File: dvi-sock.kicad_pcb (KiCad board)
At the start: 2 copper layers, 25.2 x 22.5 mm, 12 parts, among them J1 Conn_01x05, J2 Conn_01x05, J3 Conn_01x03, J4 NOT_HDMI_A

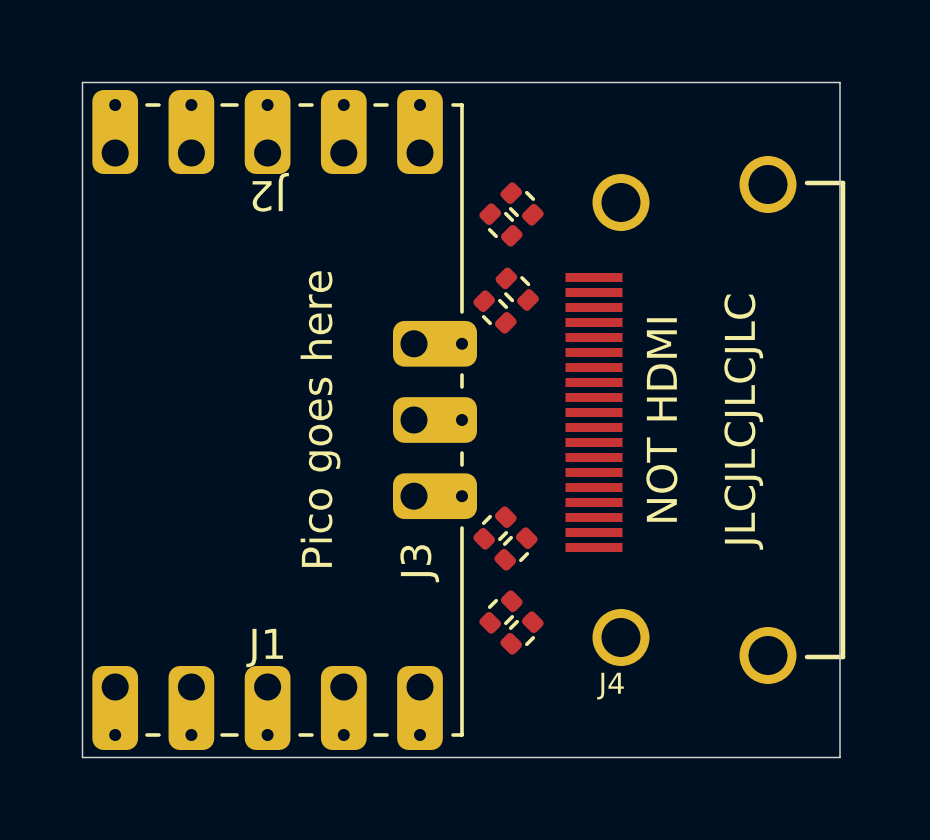
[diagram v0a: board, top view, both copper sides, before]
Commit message: Routed, DRC clean
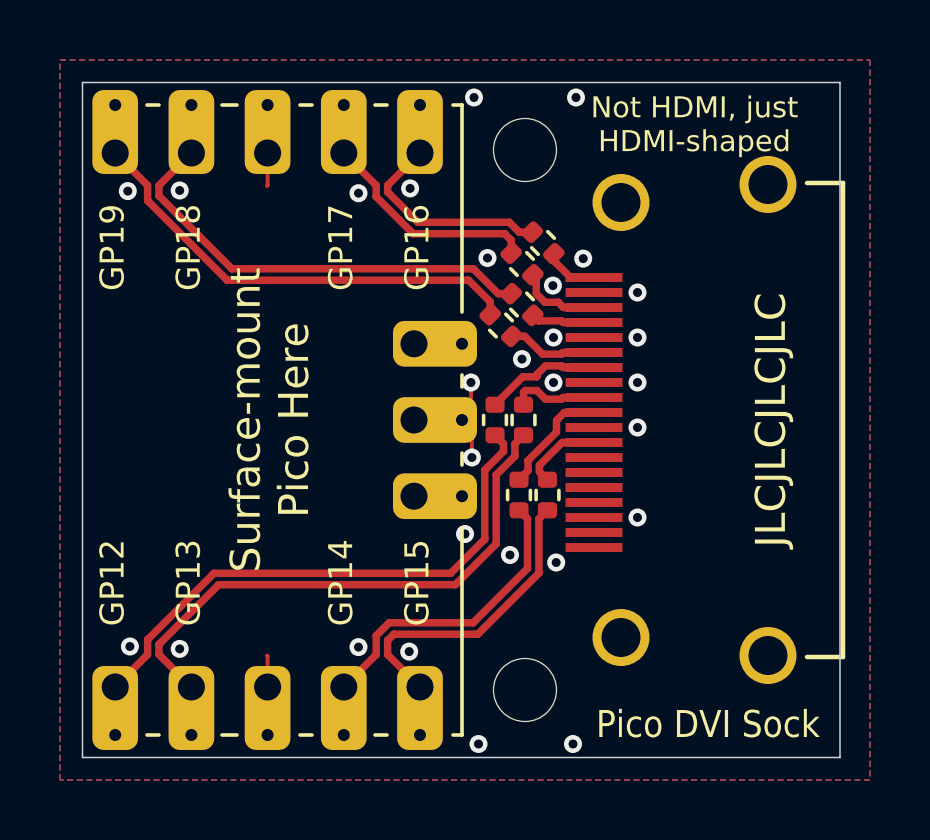
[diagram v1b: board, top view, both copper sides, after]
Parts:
- added REF**: MH_Pico_M2ish, dvi-sock:MH_Pico_M2ish, F.Cu at (156.5, 94.0)
- added REF**: MH_Pico_M2ish, dvi-sock:MH_Pico_M2ish, F.Cu at (156.5, 76.0)
- moved R8 4.68 mm to (157.2, 87.5), turned to 90 degrees
- moved R6 4.31 mm to (156.4, 85.0), turned to 90 degrees
- moved R7 3.95 mm to (156.3, 87.5), turned to 90 degrees
- moved R5 3.60 mm to (155.5, 85.0), turned to 90 degrees
- moved R2 1.48 mm to (156.4, 79.8)
- moved R1 1.48 mm to (157.1, 79.1)
- moved R3 0.54 mm to (156.4, 81.2)
- moved R4 0.49 mm to (155.7, 81.8)
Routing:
- net /PICO_D0+: track 0.00 -> 18.5 mm
- net /PICO_D0-: track 0.00 -> 18.5 mm
- net /PICO_D1-: track 0.00 -> 15.3 mm
- net /PICO_D1+: track 0.00 -> 15.0 mm
- net /PICO_CK-: track 0.00 -> 10.2 mm
- net /PICO_CK+: track 0.00 -> 10.2 mm
- net /PICO_D2-: track 0.00 -> 7.44 mm
- net /PICO_D2+: track 0.00 -> 7.12 mm
- net GND: track 0.00 -> 4.93 mm, vias 0 -> 28
- net /D0+: track 0.00 -> 3.90 mm
- net /CK+: track 0.00 -> 3.85 mm
- net /D1-: track 0.00 -> 3.01 mm
- net /D2-: track 0.00 -> 2.99 mm
- net /D0-: track 0.00 -> 2.93 mm
- net /CK-: track 0.00 -> 2.73 mm
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- added copper zone on B.Cu, net GND
- added copper zone on F.Cu, net GND
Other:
- board text added: "GP12"
- board text added: "GP12: D0+ GP13: D0- GP14: CK+ GP15: CK- GP16: D2+ GP17: D2- GP18: D1+ GP19: D1-"
- board text added: "GP13"
- board text added: "GP14"
- board text added: "GP15"
- board text added: "GP16"
- board text added: "GP17"
- board text added: "GP18"
- board text added: "GP19"
- board text added: "Not HDMI, just HDMI-shaped"
- board text added: "Pico DVI Sock"
- board text added: "Surface-mount Pico Here"
- board text removed: "Pico goes here"

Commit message: Rounded corners, license, readme
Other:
- outline, holes or cut-outs redrawn
- board text added: "Rev A"
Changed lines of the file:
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@@
   (gr_line (start 154.4 95.5) (end 154.1 95.5) (layer "F.SilkS") (width 0.12))
   (gr_line (start 146.4 95.5) (end 146.9 95.5) (layer "F.SilkS") (width 0.12))
-  (gr_line (start 167 96.25) (end 141.75 96.25) (layer "Edge.Cuts") (width 0.05))
-  (gr_line (start 141.75 73.75) (end 167 73.75) (layer "Edge.Cuts") (width 0.05))
-  (gr_line (start 141.75 96.25) (end 141.75 73.75) (layer "Edge.Cuts") (width 0.05))
-  (gr_line (start 167 73.75) (end 167 96.25) (layer "Edge.Cuts") (width 0.05))
+  (gr_arc (start 142.25 95.75) (end 142.25 96.25) (angle 90) (layer "Edge.Cuts") (width 0.05))
+  (gr_line (start 166.5 96.25) (end 142.25 96.25) (layer "Edge.Cuts") (width 0.05))
+  (gr_line (start 142.25 73.75) (end 166.5 73.75) (layer "Edge.Cuts") (width 0.05))
+  (gr_arc (start 166.5 74.25) (end 166.5 73.75) (angle 90) (layer "Edge.Cuts") (width 0.05))
+  (gr_arc (start 166.5 95.75) (end 167 95.75) (angle 90) (layer "Edge.Cuts") (width 0.05))
+  (gr_line (start 141.75 95.75) (end 141.75 74.25) (layer "Edge.Cuts") (width 0.05))
+  (gr_line (start 167 74.25) (end 167 95.75) (layer "Edge.Cuts") (width 0.05))
+  (gr_arc (start 142.25 74.25) (end 142.25 73.75) (angle -90) (layer "Edge.Cuts") (width 0.05))
   (gr_text "NOT HDMI" (at 163 85 90) (layer "B.SilkS")
     (effects (font (size 1 1) (thickness 0.25)) (justify mirror))
@@
     (effects (font (size 1 1) (thickness 0.15)) (justify mirror))
   )
+  (gr_text "Rev A" (at 162.25 95) (layer "B.SilkS")
+    (effects (font (size 0.7 0.7) (thickness 0.12)) (justify mirror))
+  )
   (gr_text "Pico DVI Sock" (at 162.6 95.15) (layer "F.SilkS")

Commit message: Oops, missing via
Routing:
- net GND: vias 28 -> 29
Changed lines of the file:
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@@
   (via (at 143.33 92.55) (size 0.6) (drill 0.3) (layers "F.Cu" "B.Cu") (free) (net 3))
   (via (at 157.45 83.75) (size 0.6) (drill 0.3) (layers "F.Cu" "B.Cu") (free) (net 3))
+  (via (at 154.6 81.2) (size 0.6) (drill 0.3) (layers "F.Cu" "B.Cu") (free) (net 3))
   (via (at 154.95 95.8) (size 0.6) (drill 0.3) (layers "F.Cu" "B.Cu") (free) (net 3))
   (via (at 156.4 82.97) (size 0.6) (drill 0.3) (layers "F.Cu" "B.Cu") (free) (net 3))
